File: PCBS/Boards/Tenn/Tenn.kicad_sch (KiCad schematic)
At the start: 34 parts, among them J1 Conn_01x02_Socket, J10 Conn_01x03_Male, J11 Conn_01x03_Male, J12 Conn_01x04_Female, J13 Conn_01x03_Male, J14 Conn_01x03_Male, J15 Conn_01x03_Male, J16 Conn_01x02_Male, J17 Conn_01x02_Male, J2 Conn_01x03_Male, J3 Conn_01x03_Male, J4 Conn_01x03_Male, J5 Conn_01x03_Male, J6 Conn_01x03_Male, J7 Conn_01x03_Male, J8 Conn_01x03_Male, J9 Conn_01x03_Male, SW2 SW_Push, SW3 SW_Push, SW4 SW_SPDT, U1 L7805, U2 DRV8871DDA, U3 DRV8871DDA

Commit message: updated README
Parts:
- J12: footprint Connector_PinHeader_2.54mm:PinHeader_1x04_P2.54mm_Vertical -> Connector_PinSocket_2.54mm:PinSocket_1x04_P2.54mm_Vertical
- J16, J17: footprint Connector_PinSocket_2.54mm:PinSocket_1x02_P2.54mm_Vertical -> Connector_JST:JST_XH_B2B-XH-A_1x02_P2.50mm_Vertical
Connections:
- net SCL: now also A1.24 (A5); no longer A1.22 (A3)
- net SDA: now also A1.23 (A4); no longer A1.21 (A2)
- net Sens6: now also A1.21 (A2); no longer A1.23 (A4)
- net Sens7: now also A1.22 (A3); no longer A1.24 (A5)
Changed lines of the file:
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@@
     )
   )
-  (global_label "SDA" (shape input) (at 175.26 115.57 0) (fields_autoplaced)
+  (global_label "SDA" (shape input) (at 175.26 120.65 0) (fields_autoplaced)
     (effects (font (size 1.27 1.27)) (justify left))
-    (property "Intersheetrefs" "${INTERSHEET_REFS}" (at 181.2412 115.4906 0)
+    (property "Intersheetrefs" "${INTERSHEET_REFS}" (at 181.2412 120.5706 0)
       (effects (font (size 1.27 1.27)) (justify left) hide)
     )
@@
     )
   )
-  (global_label "Sens6" (shape input) (at 175.26 120.65 0) (fields_autoplaced)
+  (global_label "Sens6" (shape input) (at 175.26 115.57 0) (fields_autoplaced)
     (effects (font (size 1.27 1.27)) (justify left))
-    (property "Intersheetrefs" "${INTERSHEET_REFS}" (at 183.3579 120.5706 0)
+    (property "Intersheetrefs" "${INTERSHEET_REFS}" (at 183.3579 115.4906 0)
       (effects (font (size 1.27 1.27)) (justify left) hide)
     )
@@
     )
   )
-  (global_label "SCL" (shape input) (at 175.26 118.11 0) (fields_autoplaced)
+  (global_label "SCL" (shape input) (at 175.26 123.19 0) (fields_autoplaced)
     (effects (font (size 1.27 1.27)) (justify left))
-    (property "Intersheetrefs" "${INTERSHEET_REFS}" (at 181.1807 118.0306 0)
+    (property "Intersheetrefs" "${INTERSHEET_REFS}" (at 181.1807 123.1106 0)
       (effects (font (size 1.27 1.27)) (justify left) hide)
     )
   )
-  (global_label "Sens7" (shape input) (at 175.26 123.19 0) (fields_autoplaced)
+  (global_label "Sens7" (shape input) (at 175.26 118.11 0) (fields_autoplaced)
     (effects (font (size 1.27 1.27)) (justify left))
-    (property "Intersheetrefs" "${INTERSHEET_REFS}" (at 183.3579 123.1106 0)
+    (property "Intersheetrefs" "${INTERSHEET_REFS}" (at 183.3579 118.0306 0)
       (effects (font (size 1.27 1.27)) (justify left) hide)
     )
@@
       (effects (font (size 1.27 1.27)))
     )
-    (property "Footprint" "Connector_PinSocket_2.54mm:PinSocket_1x02_P2.54mm_Vertical" (at 213.36 130.81 0)
+    (property "Footprint" "Connector_JST:JST_XH_B2B-XH-A_1x02_P2.50mm_Vertical" (at 213.36 130.81 0)
       (effects (font (size 1.27 1.27)) hide)
     )
@@
       (effects (font (size 1.27 1.27)))
     )
-    (property "Footprint" "Connector_PinSocket_2.54mm:PinSocket_1x02_P2.54mm_Vertical" (at 214.63 93.98 0)
+    (property "Footprint" "Connector_JST:JST_XH_B2B-XH-A_1x02_P2.50mm_Vertical" (at 214.63 93.98 0)
       (effects (font (size 1.27 1.27)) hide)
     )
@@
       (effects (font (size 1.27 1.27)))
     )
-    (property "Footprint" "Connector_PinHeader_2.54mm:PinHeader_1x04_P2.54mm_Vertical" (at 99.06 90.17 0)
-      (effects (font (size 1.27 1.27)) hide)
-    )
+    (property "Footprint" "Connector_PinSocket_2.54mm:PinSocket_1x04_P2.54mm_Vertical" (at 99.06 90.17 0)
+      (effects (font (size 1.27 1.27)) hide)
+    )

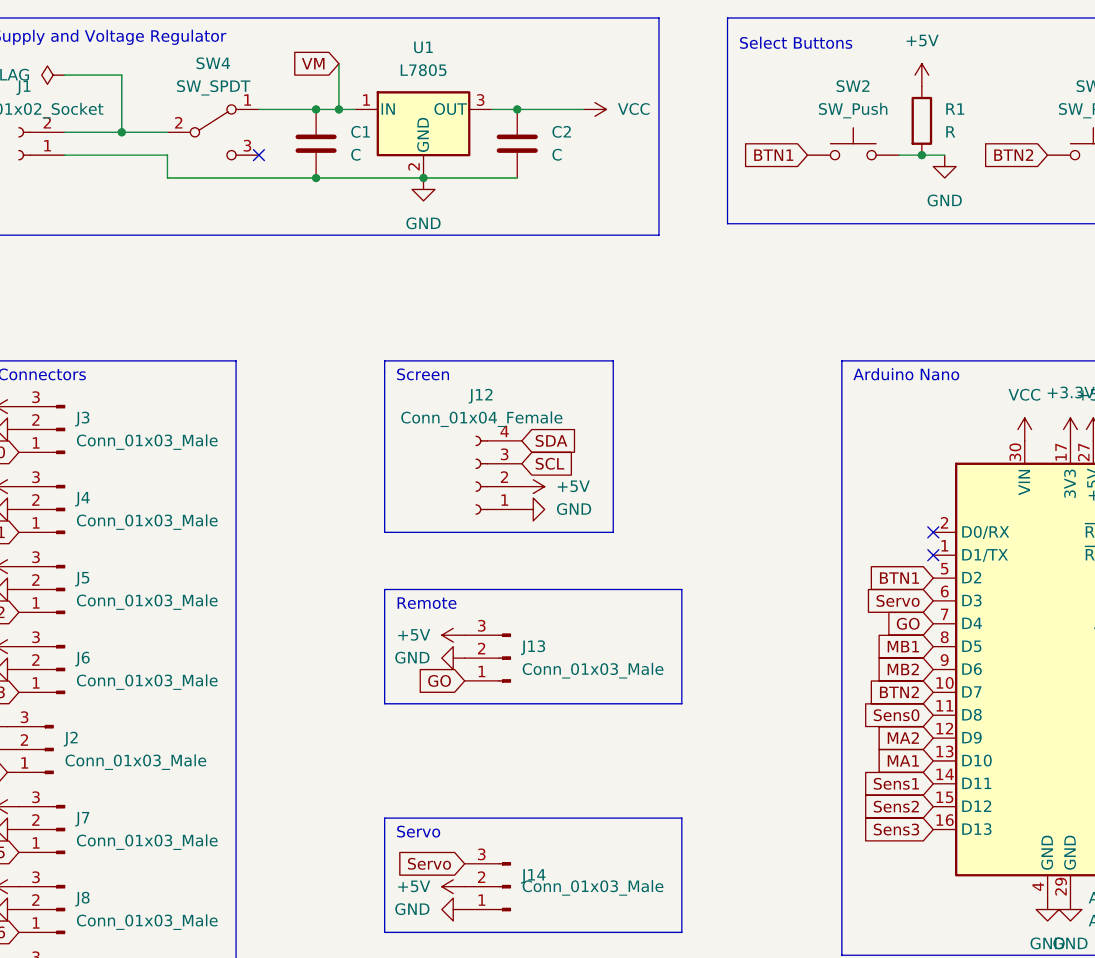
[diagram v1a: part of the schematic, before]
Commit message: Updates nets and adds tracks in pcb file
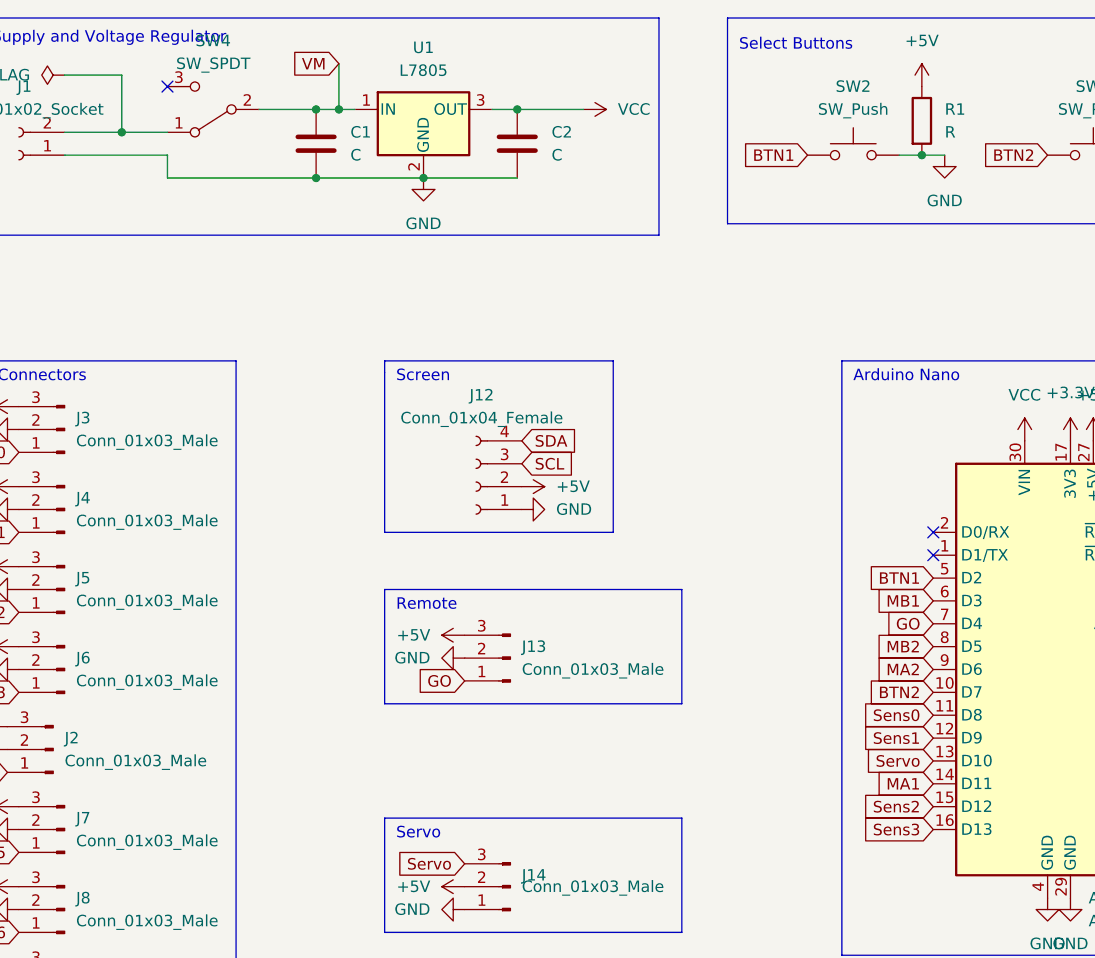
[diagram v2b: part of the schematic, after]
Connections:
- net MA1: now also A1.14 (D11); no longer A1.13 (D10)
- net MA2: now also A1.9 (D6); no longer A1.12 (D9)
- net MB1: now also A1.6 (D3); no longer A1.8 (D5)
- net MB2: now also A1.8 (D5); no longer A1.9 (D6)
- net Sens1: now also A1.12 (D9); no longer A1.14 (D11)
- net Servo: now also A1.13 (D10); no longer A1.6 (D3)
- net VM: now also SW4.2 (B); no longer SW4.1 (A)
- net at J1.2 (Pin_2): now also SW4.1 (A); no longer SW4.2 (B)
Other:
- moved on the sheet: SW4
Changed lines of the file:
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@@
   (no_connect (at 149.86 97.79))
   (no_connect (at 149.86 95.25))
-  (no_connect (at 74.93 53.34))
+  (no_connect (at 64.77 45.72))
   (wire (pts (xy 238.76 146.05) (xy 243.84 146.05))
     (stroke (width 0) (type default))
@@
     )
   )
-  (global_label "MA1" (shape input) (at 149.86 120.65 180) (fields_autoplaced)
-    (effects (font (size 1.27 1.27)) (justify right))
-    (property "Intersheetrefs" "${INTERSHEET_REFS}" (at 143.6974 120.5706 0)
+  (global_label "MA1" (shape input) (at 149.86 123.19 180) (fields_autoplaced)
+    (effects (font (size 1.27 1.27)) (justify right))
+    (property "Intersheetrefs" "${INTERSHEET_REFS}" (at 143.6974 123.1106 0)
       (effects (font (size 1.27 1.27)) (justify right) hide)
     )
@@
     )
   )
-  (global_label "MB2" (shape input) (at 149.86 110.49 180) (fields_autoplaced)
-    (effects (font (size 1.27 1.27)) (justify right))
-    (property "Intersheetrefs" "${INTERSHEET_REFS}" (at 143.5159 110.4106 0)
+  (global_label "MB2" (shape input) (at 149.86 107.95 180) (fields_autoplaced)
+    (effects (font (size 1.27 1.27)) (justify right))
+    (property "Intersheetrefs" "${INTERSHEET_REFS}" (at 143.5159 107.8706 0)
       (effects (font (size 1.27 1.27)) (justify right) hide)
     )
@@
     )
   )
-  (global_label "MB1" (shape input) (at 149.86 107.95 180) (fields_autoplaced)
-    (effects (font (size 1.27 1.27)) (justify right))
-    (property "Intersheetrefs" "${INTERSHEET_REFS}" (at 143.5159 107.8706 0)
+  (global_label "MB1" (shape input) (at 149.86 102.87 180) (fields_autoplaced)
+    (effects (font (size 1.27 1.27)) (justify right))
+    (property "Intersheetrefs" "${INTERSHEET_REFS}" (at 143.5159 102.7906 0)
       (effects (font (size 1.27 1.27)) (justify right) hide)
     )
@@
     )
   )
-  (global_label "MA2" (shape input) (at 149.86 118.11 180) (fields_autoplaced)
-    (effects (font (size 1.27 1.27)) (justify right))
-    (property "Intersheetrefs" "${INTERSHEET_REFS}" (at 143.6974 118.0306 0)
+  (global_label "MA2" (shape input) (at 149.86 110.49 180) (fields_autoplaced)
+    (effects (font (size 1.27 1.27)) (justify right))
+    (property "Intersheetrefs" "${INTERSHEET_REFS}" (at 143.6974 110.4106 0)
       (effects (font (size 1.27 1.27)) (justify right) hide)
     )
@@
     )
   )
-  (global_label "Servo" (shape input) (at 149.86 102.87 180) (fields_autoplaced)
-    (effects (font (size 1.27 1.27)) (justify right))
-    (property "Intersheetrefs" "${INTERSHEET_REFS}" (at 142.2459 102.7906 0)
+  (global_label "Servo" (shape input) (at 149.86 120.65 180) (fields_autoplaced)
+    (effects (font (size 1.27 1.27)) (justify right))
+    (property "Intersheetrefs" "${INTERSHEET_REFS}" (at 142.2459 120.5706 0)
       (effects (font (size 1.27 1.27)) (justify right) hide)
     )
@@
     )
   )
-  (global_label "Sens1" (shape input) (at 149.86 123.19 180) (fields_autoplaced)
-    (effects (font (size 1.27 1.27)) (justify right))
-    (property "Intersheetrefs" "${INTERSHEET_REFS}" (at 141.7621 123.1106 0)
+  (global_label "Sens1" (shape input) (at 149.86 118.11 180) (fields_autoplaced)
+    (effects (font (size 1.27 1.27)) (justify right))
+    (property "Intersheetrefs" "${INTERSHEET_REFS}" (at 141.7621 118.0306 0)
       (effects (font (size 1.27 1.27)) (justify right) hide)
     )
@@
     )
   )
+  (netclass_flag "" (length 2.54) (shape round) (at 219.71 96.52 180) (fields_autoplaced)
+    (effects (font (size 1.27 1.27)) (justify right bottom))
+    (property "BatV" "" (at 220.4085 99.06 0) (show_name)
+      (effects (font (size 1.27 1.27) italic) (justify left))
+    )
+  )
+  (netclass_flag "" (length 2.54) (shape round) (at 219.71 93.98 0) (fields_autoplaced)
+    (effects (font (size 1.27 1.27)) (justify left bottom))
+    (property "BatV" "" (at 220.4085 91.44 0) (show_name)
+      (effects (font (size 1.27 1.27) italic) (justify left))
+    )
+  )
+  (netclass_flag "" (length 2.54) (shape round) (at 218.44 130.81 0) (fields_autoplaced)
+    (effects (font (size 1.27 1.27)) (justify left bottom))
+    (property "BatV" "" (at 219.1385 128.27 0) (show_name)
+      (effects (font (size 1.27 1.27) italic) (justify left))
+    )
+  )
+  (netclass_flag "" (length 2.54) (shape round) (at 218.44 133.35 180) (fields_autoplaced)
+    (effects (font (size 1.27 1.27)) (justify right bottom))
+    (property "BatV" "" (at 219.1385 135.89 0) (show_name)
+      (effects (font (size 1.27 1.27) italic) (justify left))
+    )
+  )
   (netclass_flag "" (length 2.54) (shape round) (at 62.23 50.8 0) (fields_autoplaced)
     (effects (font (size 1.27 1.27)) (justify left bottom))
-    (property "BatV" "BatV" (at 62.9285 48.26 0)
+    (property "BatV" "" (at 62.9285 48.26 0) (show_name)
       (effects (font (size 1.27 1.27) italic) (justify left))
     )
@@
   (netclass_flag "" (length 2.54) (shape round) (at 76.2 48.26 0) (fields_autoplaced)
     (effects (font (size 1.27 1.27)) (justify left bottom))
-    (property "BatV" "BatV" (at 76.8985 45.72 0)
+    (property "BatV" "" (at 76.8985 45.72 0) (show_name)
       (effects (font (size 1.27 1.27) italic) (justify left))
     )
@@
     )
   )
-  (symbol (lib_id "Switch:SW_SPDT") (at 69.85 50.8 0) (unit 1)
-    (in_bom yes) (on_board yes) (dnp no) (fields_autoplaced)
-    (property "Reference" "SW4" (at 69.85 43.18 0)
-      (effects (font (size 1.27 1.27)))
-    )
-    (property "Value" "SW_SPDT" (at 69.85 45.72 0)
-      (effects (font (size 1.27 1.27)))
-    )
-    (property "Footprint" "Button_Switch_SMD:SW_SPDT_PCM12" (at 69.85 50.8 0)
-      (effects (font (size 1.27 1.27)) hide)
-    )
-    (property "Datasheet" "~" (at 69.85 50.8 0)
-      (effects (font (size 1.27 1.27)) hide)
-    )
+  (symbol (lib_id "Switch:SW_SPDT") (at 69.85 48.26 180) (unit 1)
+    (in_bom yes) (on_board yes) (dnp no) (fields_autoplaced)
+    (property "Reference" "SW4" (at 69.85 40.64 0)
+      (effects (font (size 1.27 1.27)))
+    )
+    (property "Value" "SW_SPDT" (at 69.85 43.18 0)
+      (effects (font (size 1.27 1.27)))
+    )
+    (property "Footprint" "Button_Switch_SMD:SW_SPDT_PCM12" (at 69.85 48.26 0)
+      (effects (font (size 1.27 1.27)) hide)
+    )
+    (property "Datasheet" "~" (at 69.85 48.26 0)
+      (effects (font (size 1.27 1.27)) hide)
+    )
